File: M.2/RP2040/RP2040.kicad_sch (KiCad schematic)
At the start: 3 parts

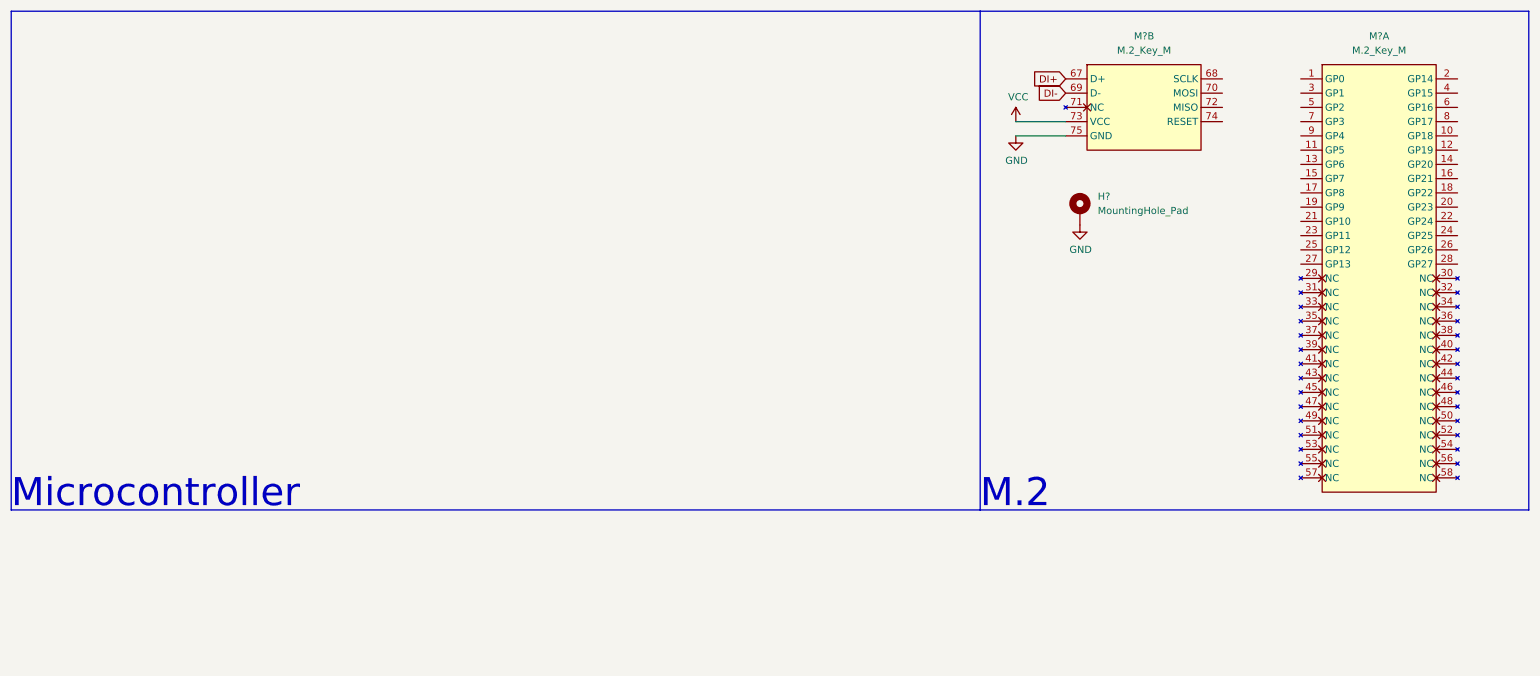
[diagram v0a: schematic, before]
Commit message: Add the files for different M.2 Boards and work on STM32F411
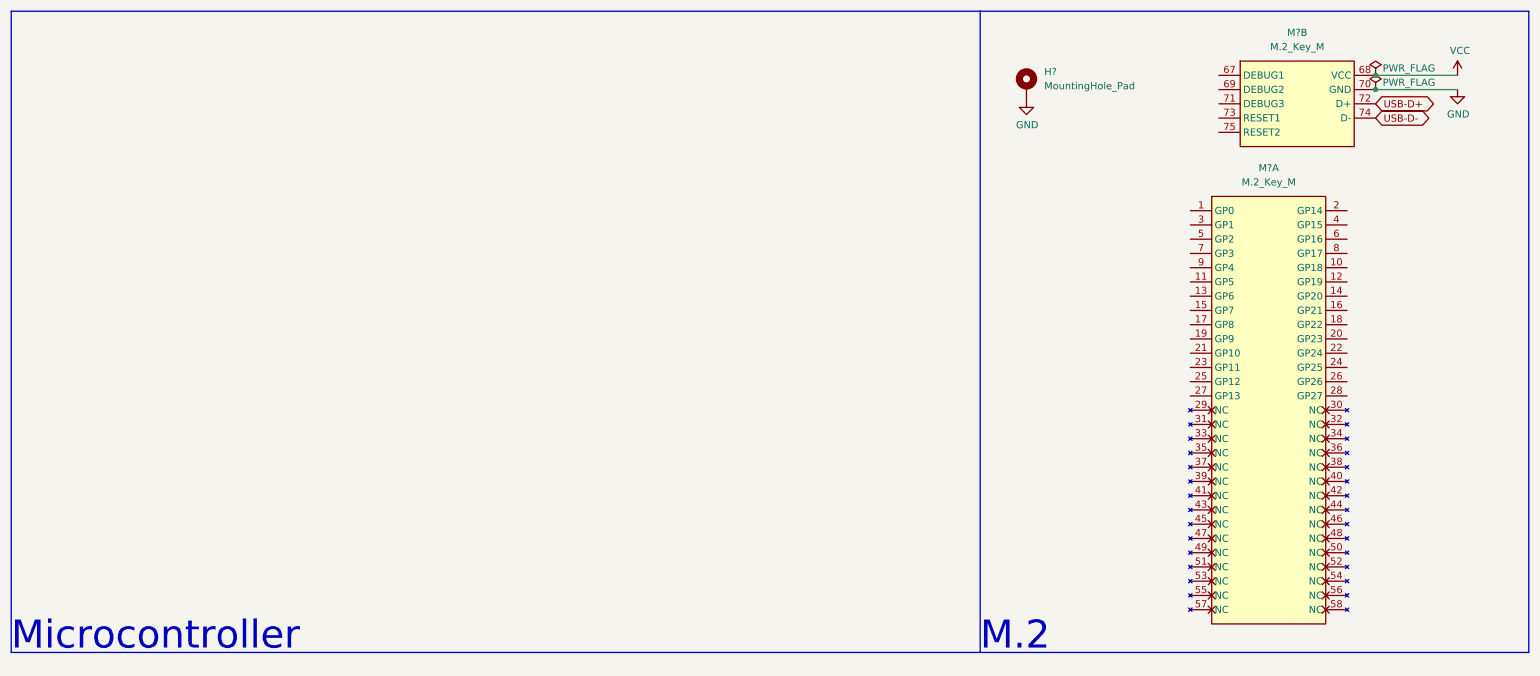
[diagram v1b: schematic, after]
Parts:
- removed H?: MountingHole_Pad, MountingHole:MountingHole_2.2mm_M2_ISO7380_Pad, symbol Mechanical:MountingHole_Pad
- removed M? (x2): M.2_Key_M, m2ngff:m2-padKeyM, symbol m2ngff:M.2_Key_M
- added H?: MountingHole_Pad, MountingHole:MountingHole_2.2mm_M2_ISO7380_Pad, symbol Mechanical:MountingHole_Pad
- added M? (x2): M.2_Key_M, m2ngff:m2-padKeyM, symbol m2ngff:M.2_Key_M
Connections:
- net GND: now also H?.1, M?.70 (GND)
- net VCC: now also M?.68 (VCC)
- new net USB-D+: M?.72 (D+)
- new net USB-D-: M?.74 (D-)

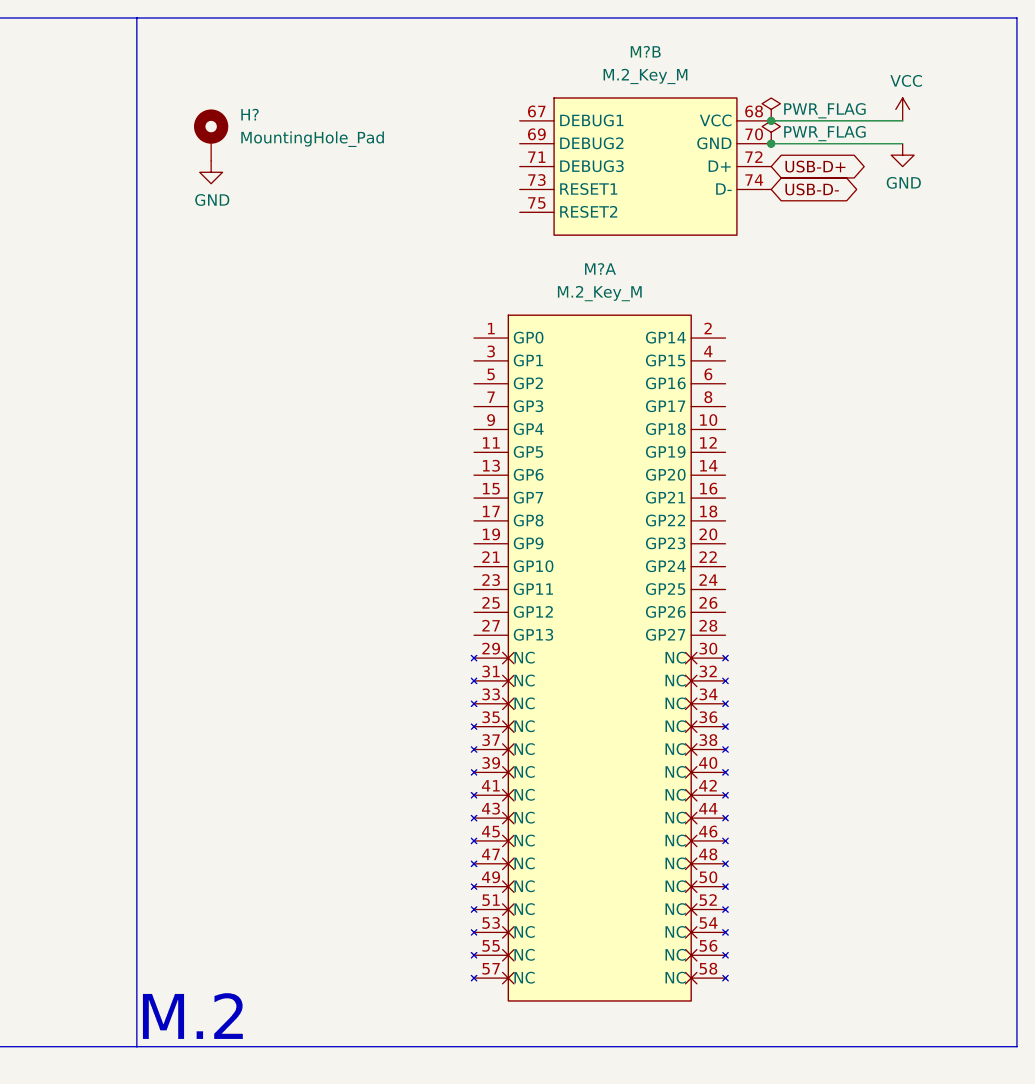
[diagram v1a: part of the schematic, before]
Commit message: change the rest to key e, change the template
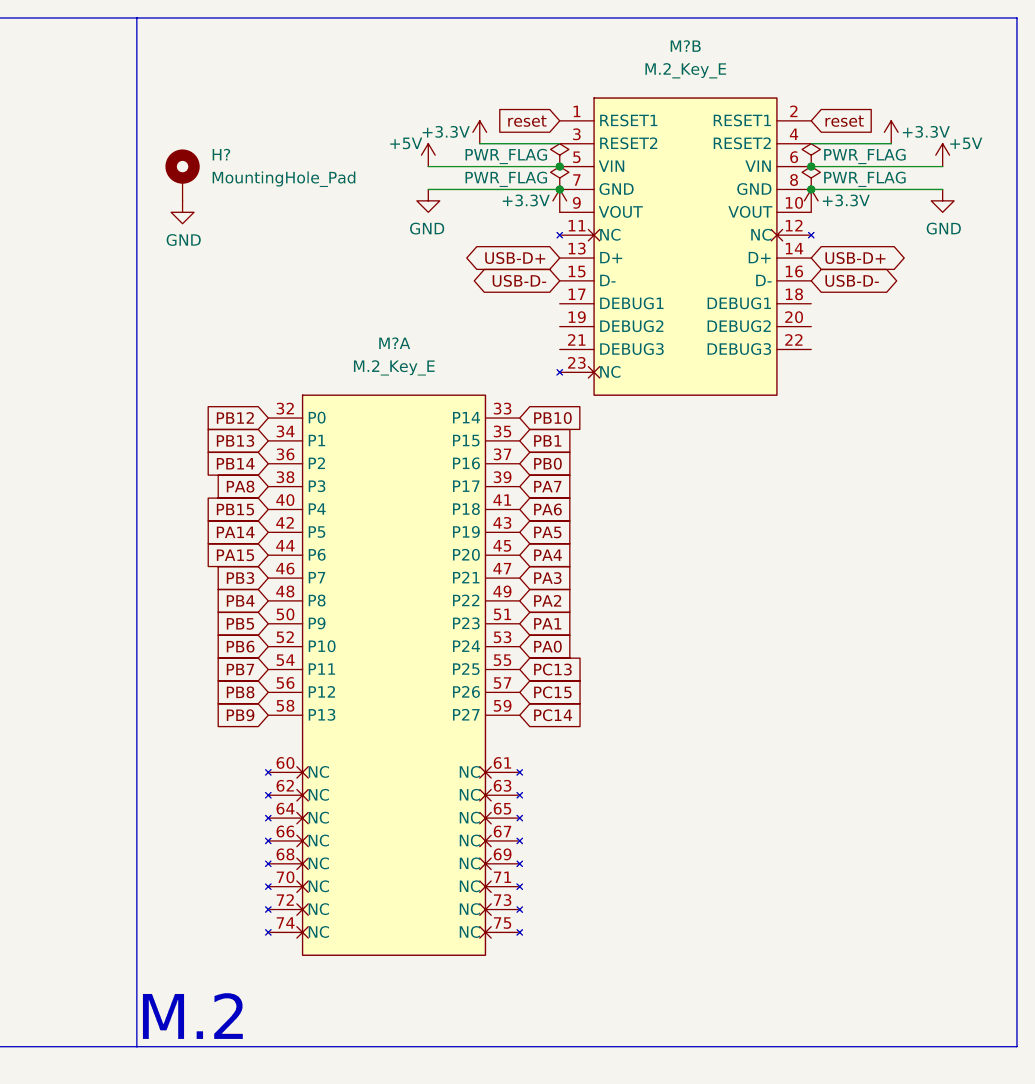
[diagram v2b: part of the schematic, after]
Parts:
- removed H?: MountingHole_Pad, MountingHole:MountingHole_2.2mm_M2_ISO7380_Pad, symbol Mechanical:MountingHole_Pad
- removed M? (x2): M.2_Key_M, m2ngff:m2-padKeyM, symbol m2ngff:M.2_Key_M
- added H?: MountingHole_Pad, MountingHole:MountingHole_2.2mm_M2_ISO7380_Pad, symbol Mechanical:MountingHole_Pad
- added M? (x2): M.2_Key_E, m2ngff:m2-padKeyE, symbol m2ngff:M.2_Key_E
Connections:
- net GND: now also H?.1, M?.7 (GND), M?.8 (GND)
- net USB-D+: now also M?.13 (D+), M?.14 (D+)
- net USB-D-: now also M?.15 (D-), M?.16 (D-)
- new net +3V3: M?.10 (VOUT), M?.3 (RESET2), M?.4 (RESET2), M?.9 (VOUT)
- new net +5V: M?.5 (VIN), M?.6 (VIN)
- new net PA0: M?.53 (P24)
- new net PA1: M?.51 (P23)
- new net PA14: M?.42 (P5)
- new net PA15: M?.44 (P6)
- new net PA2: M?.49 (P22)
- new net PA3: M?.47 (P21)
- new net PA4: M?.45 (P20)
- new net PA5: M?.43 (P19)
- new net PA6: M?.41 (P18)
- new net PA7: M?.39 (P17)
- new net PA8: M?.38 (P3)
- new net PB0: M?.37 (P16)
- new net PB1: M?.35 (P15)
- new net PB10: M?.33 (P14)
- new net PB12: M?.32 (P0)
- new net PB13: M?.34 (P1)
- new net PB14: M?.36 (P2)
- new net PB15: M?.40 (P4)
- new net PB3: M?.46 (P7)
- new net PB4: M?.48 (P8)
- new net PB5: M?.50 (P9)
- new net PB6: M?.52 (P10)
- new net PB7: M?.54 (P11)
- new net PB8: M?.56 (P12)
- new net PB9: M?.58 (P13)
- new net PC13: M?.55 (P25)
- new net PC14: M?.59 (P27)
- new net PC15: M?.57 (P26)
- new net reset: M?.1 (RESET1), M?.2 (RESET1)

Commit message: finish working on stmf411
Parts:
- removed H?: MountingHole_Pad, MountingHole:MountingHole_2.2mm_M2_ISO7380_Pad, symbol Mechanical:MountingHole_Pad
- added H?: MountingHole_Pad, MountingHole:MountingHole_2.2mm_M2_Pad_Via, symbol Mechanical:MountingHole_Pad
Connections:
- net GND: now also H?.1
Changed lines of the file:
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@@
+    (pin "1")
+  )
+  (symbol (lib_id "Power:GND") (at 189.865 28.575 0) (unit 1)
+    (in_bom yes) (on_board yes)
+    (property "Reference" "#PWR?" (id 0) (at 189.865 34.925 0)
+      (effects (font (size 1.27 1.27)) hide)
+    )
+    (property "Value" "GND" (id 1) (at 189.992 32.9692 0))
+    (property "Footprint" "" (id 2) (at 189.865 28.575 0)
+      (effects (font (size 1.27 1.27)) hide)
+    )
+    (property "Datasheet" "" (id 3) (at 189.865 28.575 0)
+      (effects (font (size 1.27 1.27)) hide)
+    )
     (pin "1")
   )
@@
     (pin "1")
   )
-  (symbol (lib_id "Mechanical:MountingHole_Pad") (at 191.135 31.115 0) (unit 1)
-    (in_bom yes) (on_board yes) (fields_autoplaced)
-    (property "Reference" "H?" (id 0) (at 194.31 28.5749 0)
-      (effects (font (size 1.27 1.27)) (justify left))
-    )
-    (property "Value" "MountingHole_Pad" (id 1) (at 194.31 31.1149 0)
-      (effects (font (size 1.27 1.27)) (justify left))
-    )
-    (property "Footprint" "MountingHole:MountingHole_2.2mm_M2_ISO7380_Pad" (id 2) (at 191.135 31.115 0)
-      (effects (font (size 1.27 1.27)) hide)
-    )
-    (property "Datasheet" "~" (id 3) (at 191.135 31.115 0)
-      (effects (font (size 1.27 1.27)) hide)
-    )
-    (pin "1")
-  )
   (symbol (lib_id "power:+3.3V") (at 269.875 27.305 0) (unit 1)
     (in_bom yes) (on_board yes)
@@
     )
     (property "Datasheet" "" (id 3) (at 275.59 29.845 0)
-      (effects (font (size 1.27 1.27)) hide)
-    )
-    (pin "1")
-  )
-  (symbol (lib_id "Power:GND") (at 191.135 33.655 0) (unit 1)
-    (in_bom yes) (on_board yes)
-    (property "Reference" "#PWR?" (id 0) (at 191.135 40.005 0)
-      (effects (font (size 1.27 1.27)) hide)
-    )
-    (property "Value" "GND" (id 1) (at 191.262 38.0492 0))
-    (property "Footprint" "" (id 2) (at 191.135 33.655 0)
-      (effects (font (size 1.27 1.27)) hide)
-    )
-    (property "Datasheet" "" (id 3) (at 191.135 33.655 0)
       (effects (font (size 1.27 1.27)) hide)
     )
@@
     (pin "9")
   )
+  (symbol (lib_id "Mechanical:MountingHole_Pad") (at 189.865 26.035 0) (unit 1)
+    (in_bom yes) (on_board yes) (fields_autoplaced)
+    (property "Reference" "H?" (id 0) (at 193.04 23.4949 0)
+      (effects (font (size 1.27 1.27)) (justify left))
+    )
+    (property "Value" "MountingHole_Pad" (id 1) (at 193.04 26.0349 0)
+      (effects (font (size 1.27 1.27)) (justify left))
+    )
+    (property "Footprint" "MountingHole:MountingHole_2.2mm_M2_Pad_Via" (id 2) (at 189.865 26.035 0)
+      (effects (font (size 1.27 1.27)) hide)
+    )
+    (property "Datasheet" "~" (id 3) (at 189.865 26.035 0)
+      (effects (font (size 1.27 1.27)) hide)
+    )
+    (pin "1")
+  )
   (symbol (lib_id "power:+3.3V") (at 224.155 27.305 0) (mirror y) (unit 1)
     (in_bom yes) (on_board yes)
@@
       (reference "#FLG?") (unit 1) (value "PWR_FLAG") (footprint "")
     )
+    (path "/29ec1a54-dea0-4d1a-a3dc-a7441a09bb9e"
+      (reference "#PWR?") (unit 1) (value "GND") (footprint "")
+    )
     (path "/2b3e8080-6e59-452f-841b-e804bf3dea49"
       (reference "#PWR?") (unit 1) (value "+5V") (footprint "")
@@
       (reference "#PWR?") (unit 1) (value "+5V") (footprint "")
     )
-    (path "/da74547b-896f-459c-8aa8-f161d000dade"
-      (reference "#PWR?") (unit 1) (value "GND") (footprint "")
-    )
     (path "/f75ad864-f096-4907-b31d-1a5733db4331"
       (reference "#PWR?") (unit 1) (value "+3.3V") (footprint "")
     )
-    (path "/7055685d-2e9b-46e1-bc20-a497c53cfccc"
-      (reference "H?") (unit 1) (value "MountingHole_Pad") (footprint "MountingHole:MountingHole_2.2mm_M2_ISO7380_Pad")
+    (path "/f205e125-3760-485b-b76a-dc2502dc5679"
+      (reference "H?") (unit 1) (value "MountingHole_Pad") (footprint "MountingHole:MountingHole_2.2mm_M2_Pad_Via")
     )
     (path "/104e71da-dfca-45be-b72b-a07760a6df68"
